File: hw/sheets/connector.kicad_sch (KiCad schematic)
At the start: 1 part, among them J1 AH58893-T9B10-3F

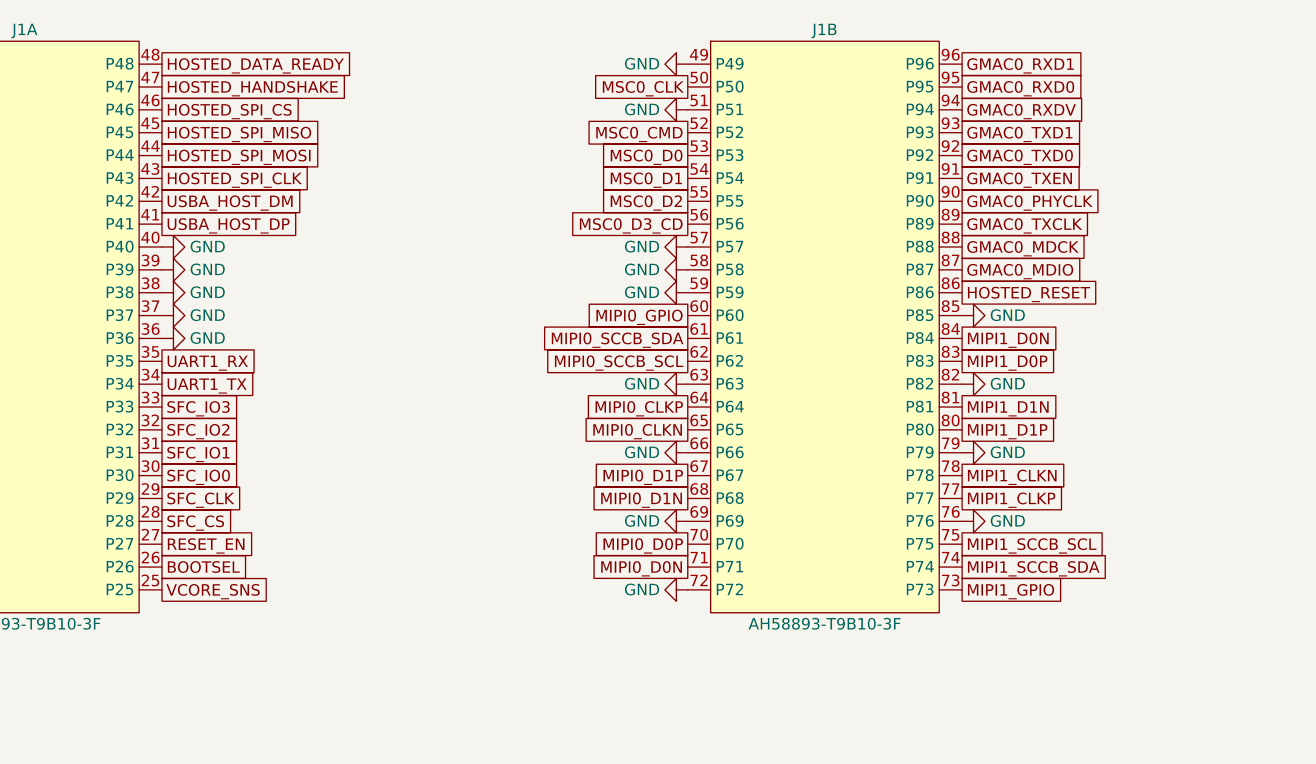
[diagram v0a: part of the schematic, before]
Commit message: Reorder J1 MSC0/USB-host/ESP-hosted/MIPI1 pins for board-order and grouping
- MSC0 (J1 pins 50/52-56): reordered to match J4's microSD pins in
  actual left-to-right board position (D1/D0/CLK/CMD/D3_CD/D2), not
  J4's raw pin numbers -- J4 sits mirrored relative to J1 on the real
  board, so matching by pin number alone produced a fully-crossed
  assignment.
- USBA_HOST_DP/DM shifted down to pins 40/41, freeing pin 42 for
  HOSTED_RESET so all ESP-Hosted signals (reset + SPI + handshake) are
  one contiguous block (42-48) instead of HOSTED_RESET sitting alone at
  unit 2 pin 86. Pin 86 is now GND.
- MIPI1 pins 73-75 rotated (GPIO/SDA/SCL -> SDA/SCL/GPIO) to match
  MIPI0's arrangement.

PCB updated to match: pad nets reassigned for all of the above, and the
already-routed MSC0/MIPI1 SDA+SCL traces had their J1-side endpoints
moved to the new pad positions rather than left stale. GND zone
refilled and DRC-clean for all touched nets.
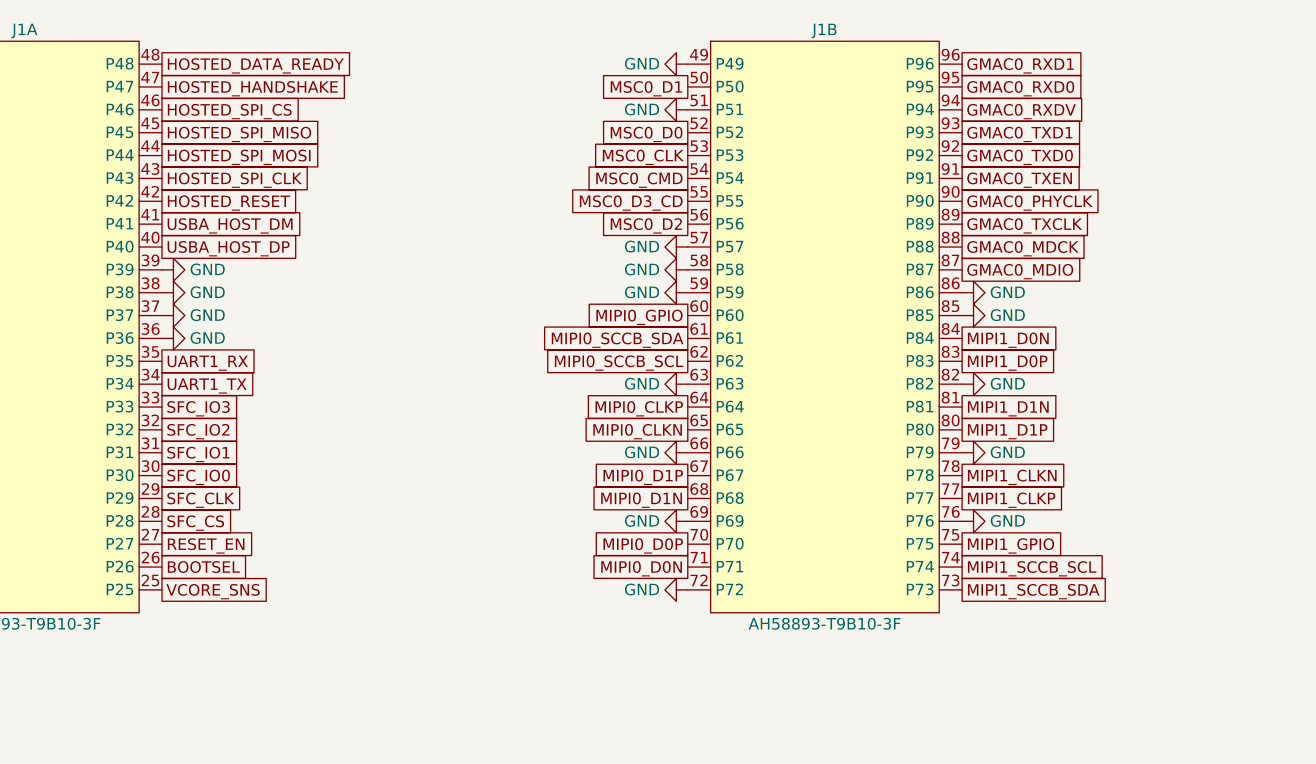
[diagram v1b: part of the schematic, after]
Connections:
- net GND: now also J1.86 (P86); no longer J1.40 (P40)
- net HOSTED_RESET: now also J1.42 (P42); no longer J1.86 (P86)
- net MIPI1_GPIO: now also J1.75 (P75); no longer J1.73 (P73)
- net MIPI1_SCCB_SCL: now also J1.74 (P74); no longer J1.75 (P75)
- net MIPI1_SCCB_SDA: now also J1.73 (P73); no longer J1.74 (P74)
- net MSC0_CLK: now also J1.53 (P53); no longer J1.50 (P50)
- net MSC0_CMD: now also J1.54 (P54); no longer J1.52 (P52)
- net MSC0_D0: now also J1.52 (P52); no longer J1.53 (P53)
- net MSC0_D1: now also J1.50 (P50); no longer J1.54 (P54)
- net MSC0_D2: now also J1.56 (P56); no longer J1.55 (P55)
- net MSC0_D3_CD: now also J1.55 (P55); no longer J1.56 (P56)
- net USBA_HOST_DM: now also J1.41 (P41); no longer J1.42 (P42)
- net USBA_HOST_DP: now also J1.40 (P40); no longer J1.41 (P41)
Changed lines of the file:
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@@
 		(property "Value" "GND" (at 71.12 64.77 270) (effects (font (size 1.27 1.27))))
-	)
-	(symbol (lib_id "power:GND") (at 66.04 62.23 90) (unit 1)
-		(property "Reference" "#CGND015" (at 66.04 62.23 0) (effects (font (size 1.27 1.27)) hide))
-		(property "Value" "GND" (at 71.12 62.23 270) (effects (font (size 1.27 1.27))))
 	)
 	(symbol (lib_id "teacup-carrier:AH58893-T9B10-3F") (at 139.7 71.12 0) (unit 2)
@@
 	)
 	(symbol (lib_id "power:GND") (at 124.46 41.91 270) (unit 1)
-		(property "Reference" "#CGND016" (at 124.46 41.91 0) (effects (font (size 1.27 1.27)) hide))
+		(property "Reference" "#CGND015" (at 124.46 41.91 0) (effects (font (size 1.27 1.27)) hide))
 		(property "Value" "GND" (at 119.38 41.91 90) (effects (font (size 1.27 1.27))))
 	)
 	(symbol (lib_id "power:GND") (at 124.46 46.99 270) (unit 1)
-		(property "Reference" "#CGND017" (at 124.46 46.99 0) (effects (font (size 1.27 1.27)) hide))
+		(property "Reference" "#CGND016" (at 124.46 46.99 0) (effects (font (size 1.27 1.27)) hide))
 		(property "Value" "GND" (at 119.38 46.99 90) (effects (font (size 1.27 1.27))))
 	)
 	(symbol (lib_id "power:GND") (at 124.46 62.23 270) (unit 1)
-		(property "Reference" "#CGND018" (at 124.46 62.23 0) (effects (font (size 1.27 1.27)) hide))
+		(property "Reference" "#CGND017" (at 124.46 62.23 0) (effects (font (size 1.27 1.27)) hide))
 		(property "Value" "GND" (at 119.38 62.23 90) (effects (font (size 1.27 1.27))))
 	)
 	(symbol (lib_id "power:GND") (at 124.46 64.77 270) (unit 1)
-		(property "Reference" "#CGND019" (at 124.46 64.77 0) (effects (font (size 1.27 1.27)) hide))
+		(property "Reference" "#CGND018" (at 124.46 64.77 0) (effects (font (size 1.27 1.27)) hide))
 		(property "Value" "GND" (at 119.38 64.77 90) (effects (font (size 1.27 1.27))))
 	)
 	(symbol (lib_id "power:GND") (at 124.46 67.31 270) (unit 1)
-		(property "Reference" "#CGND020" (at 124.46 67.31 0) (effects (font (size 1.27 1.27)) hide))
+		(property "Reference" "#CGND019" (at 124.46 67.31 0) (effects (font (size 1.27 1.27)) hide))
 		(property "Value" "GND" (at 119.38 67.31 90) (effects (font (size 1.27 1.27))))
 	)
 	(symbol (lib_id "power:GND") (at 124.46 77.47 270) (unit 1)
-		(property "Reference" "#CGND021" (at 124.46 77.47 0) (effects (font (size 1.27 1.27)) hide))
+		(property "Reference" "#CGND020" (at 124.46 77.47 0) (effects (font (size 1.27 1.27)) hide))
 		(property "Value" "GND" (at 119.38 77.47 90) (effects (font (size 1.27 1.27))))
 	)
 	(symbol (lib_id "power:GND") (at 124.46 85.09 270) (unit 1)
-		(property "Reference" "#CGND022" (at 124.46 85.09 0) (effects (font (size 1.27 1.27)) hide))
+		(property "Reference" "#CGND021" (at 124.46 85.09 0) (effects (font (size 1.27 1.27)) hide))
 		(property "Value" "GND" (at 119.38 85.09 90) (effects (font (size 1.27 1.27))))
 	)
 	(symbol (lib_id "power:GND") (at 124.46 92.71 270) (unit 1)
-		(property "Reference" "#CGND023" (at 124.46 92.71 0) (effects (font (size 1.27 1.27)) hide))
+		(property "Reference" "#CGND022" (at 124.46 92.71 0) (effects (font (size 1.27 1.27)) hide))
 		(property "Value" "GND" (at 119.38 92.71 90) (effects (font (size 1.27 1.27))))
 	)
 	(symbol (lib_id "power:GND") (at 124.46 100.33 270) (unit 1)
-		(property "Reference" "#CGND024" (at 124.46 100.33 0) (effects (font (size 1.27 1.27)) hide))
+		(property "Reference" "#CGND023" (at 124.46 100.33 0) (effects (font (size 1.27 1.27)) hide))
 		(property "Value" "GND" (at 119.38 100.33 90) (effects (font (size 1.27 1.27))))
 	)
 	(symbol (lib_id "power:GND") (at 154.94 92.71 90) (unit 1)
-		(property "Reference" "#CGND025" (at 154.94 92.71 0) (effects (font (size 1.27 1.27)) hide))
+		(property "Reference" "#CGND024" (at 154.94 92.71 0) (effects (font (size 1.27 1.27)) hide))
 		(property "Value" "GND" (at 160.02 92.71 270) (effects (font (size 1.27 1.27))))
 	)
 	(symbol (lib_id "power:GND") (at 154.94 85.09 90) (unit 1)
-		(property "Reference" "#CGND026" (at 154.94 85.09 0) (effects (font (size 1.27 1.27)) hide))
+		(property "Reference" "#CGND025" (at 154.94 85.09 0) (effects (font (size 1.27 1.27)) hide))
 		(property "Value" "GND" (at 160.02 85.09 270) (effects (font (size 1.27 1.27))))
 	)
 	(symbol (lib_id "power:GND") (at 154.94 77.47 90) (unit 1)
-		(property "Reference" "#CGND027" (at 154.94 77.47 0) (effects (font (size 1.27 1.27)) hide))
+		(property "Reference" "#CGND026" (at 154.94 77.47 0) (effects (font (size 1.27 1.27)) hide))
 		(property "Value" "GND" (at 160.02 77.47 270) (effects (font (size 1.27 1.27))))
 	)
 	(symbol (lib_id "power:GND") (at 154.94 69.85 90) (unit 1)
-		(property "Reference" "#CGND028" (at 154.94 69.85 0) (effects (font (size 1.27 1.27)) hide))
+		(property "Reference" "#CGND027" (at 154.94 69.85 0) (effects (font (size 1.27 1.27)) hide))
 		(property "Value" "GND" (at 160.02 69.85 270) (effects (font (size 1.27 1.27))))
+	)
+	(symbol (lib_id "power:GND") (at 154.94 67.31 90) (unit 1)
+		(property "Reference" "#CGND028" (at 154.94 67.31 0) (effects (font (size 1.27 1.27)) hide))
+		(property "Value" "GND" (at 160.02 67.31 270) (effects (font (size 1.27 1.27))))
 	)
 	(symbol (lib_id "teacup-carrier:AH58893-T9B10-3F") (at 228.6 71.12 0) (unit 3)
@@
 	(global_label "UART1_TX" (at 66.04 77.47 0) (effects (font (size 1.27 1.27)) (justify left)))
 	(global_label "UART1_RX" (at 66.04 74.93 0) (effects (font (size 1.27 1.27)) (justify left)))
-	(global_label "USBA_HOST_DP" (at 66.04 59.69 0) (effects (font (size 1.27 1.27)) (justify left)))
-	(global_label "USBA_HOST_DM" (at 66.04 57.15 0) (effects (font (size 1.27 1.27)) (justify left)))
+	(global_label "USBA_HOST_DP" (at 66.04 62.23 0) (effects (font (size 1.27 1.27)) (justify left)))
+	(global_label "USBA_HOST_DM" (at 66.04 59.69 0) (effects (font (size 1.27 1.27)) (justify left)))
+	(global_label "HOSTED_RESET" (at 66.04 57.15 0) (effects (font (size 1.27 1.27)) (justify left)))
 	(global_label "HOSTED_SPI_CLK" (at 66.04 54.61 0) (effects (font (size 1.27 1.27)) (justify left)))
 	(global_label "HOSTED_SPI_MOSI" (at 66.04 52.07 0) (effects (font (size 1.27 1.27)) (justify left)))
@@
 	(global_label "HOSTED_HANDSHAKE" (at 66.04 44.45 0) (effects (font (size 1.27 1.27)) (justify left)))
 	(global_label "HOSTED_DATA_READY" (at 66.04 41.91 0) (effects (font (size 1.27 1.27)) (justify left)))
-	(global_label "MSC0_CLK" (at 124.46 44.45 180) (effects (font (size 1.27 1.27)) (justify right)))
-	(global_label "MSC0_CMD" (at 124.46 49.53 180) (effects (font (size 1.27 1.27)) (justify right)))
-	(global_label "MSC0_D0" (at 124.46 52.07 180) (effects (font (size 1.27 1.27)) (justify right)))
-	(global_label "MSC0_D1" (at 124.46 54.61 180) (effects (font (size 1.27 1.27)) (justify right)))
-	(global_label "MSC0_D2" (at 124.46 57.15 180) (effects (font (size 1.27 1.27)) (justify right)))
-	(global_label "MSC0_D3_CD" (at 124.46 59.69 180) (effects (font (size 1.27 1.27)) (justify right)))
+	(global_label "MSC0_D1" (at 124.46 44.45 180) (effects (font (size 1.27 1.27)) (justify right)))
+	(global_label "MSC0_D0" (at 124.46 49.53 180) (effects (font (size 1.27 1.27)) (justify right)))
+	(global_label "MSC0_CLK" (at 124.46 52.07 180) (effects (font (size 1.27 1.27)) (justify right)))
+	(global_label "MSC0_CMD" (at 124.46 54.61 180) (effects (font (size 1.27 1.27)) (justify right)))
+	(global_label "MSC0_D3_CD" (at 124.46 57.15 180) (effects (font (size 1.27 1.27)) (justify right)))
+	(global_label "MSC0_D2" (at 124.46 59.69 180) (effects (font (size 1.27 1.27)) (justify right)))
 	(global_label "MIPI0_GPIO" (at 124.46 69.85 180) (effects (font (size 1.27 1.27)) (justify right)))
 	(global_label "MIPI0_SCCB_SDA" (at 124.46 72.39 180) (effects (font (size 1.27 1.27)) (justify right)))
@@
 	(global_label "MIPI0_D0P" (at 124.46 95.25 180) (effects (font (size 1.27 1.27)) (justify right)))
 	(global_label "MIPI0_D0N" (at 124.46 97.79 180) (effects (font (size 1.27 1.27)) (justify right)))
-	(global_label "MIPI1_GPIO" (at 154.94 100.33 0) (effects (font (size 1.27 1.27)) (justify left)))
-	(global_label "MIPI1_SCCB_SDA" (at 154.94 97.79 0) (effects (font (size 1.27 1.27)) (justify left)))
-	(global_label "MIPI1_SCCB_SCL" (at 154.94 95.25 0) (effects (font (size 1.27 1.27)) (justify left)))
+	(global_label "MIPI1_SCCB_SDA" (at 154.94 100.33 0) (effects (font (size 1.27 1.27)) (justify left)))
+	(global_label "MIPI1_SCCB_SCL" (at 154.94 97.79 0) (effects (font (size 1.27 1.27)) (justify left)))
+	(global_label "MIPI1_GPIO" (at 154.94 95.25 0) (effects (font (size 1.27 1.27)) (justify left)))
 	(global_label "MIPI1_CLKP" (at 154.94 90.17 0) (effects (font (size 1.27 1.27)) (justify left)))
 	(global_label "MIPI1_CLKN" (at 154.94 87.63 0) (effects (font (size 1.27 1.27)) (justify left)))
@@
 	(global_label "MIPI1_D0P" (at 154.94 74.93 0) (effects (font (size 1.27 1.27)) (justify left)))
 	(global_label "MIPI1_D0N" (at 154.94 72.39 0) (effects (font (size 1.27 1.27)) (justify left)))
-	(global_label "HOSTED_RESET" (at 154.94 67.31 0) (effects (font (size 1.27 1.27)) (justify left)))
 	(global_label "GMAC0_MDIO" (at 154.94 64.77 0) (effects (font (size 1.27 1.27)) (justify left)))
 	(global_label "GMAC0_MDCK" (at 154.94 62.23 0) (effects (font (size 1.27 1.27)) (justify left)))
